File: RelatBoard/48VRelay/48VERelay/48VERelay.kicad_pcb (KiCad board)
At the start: 4 copper layers, 117 x 92 mm, 110 parts, among them J1 12, J10 Screw_Terminal_01x03, J11 Screw_Terminal_01x03, J12 Screw_Terminal_01x03, J13 Screw_Terminal_01x03, J14 Screw_Terminal_01x03, J2 RJ45_Hanrun_HR911105A_Horizon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, J3 B4B-PH-SM4-TB, J5 TC2030, K10 G2RL-1-E, K11 G2RL-1-E, K12 G2RL-1-E, K13 G2RL-1-E, K14 G2RL-1-E, U1 ESP32-WROOM-32UE, U10 TLV1117LV33DCYR, U2 ULN2803A, U3 W5500, U4 3A 32V, U5 TPS630701RNMR, U7 TVS1800DRVR, U9 TLV1117LV33DCYR, Y2 ABM3C-25.000MHZ-D4Y-T

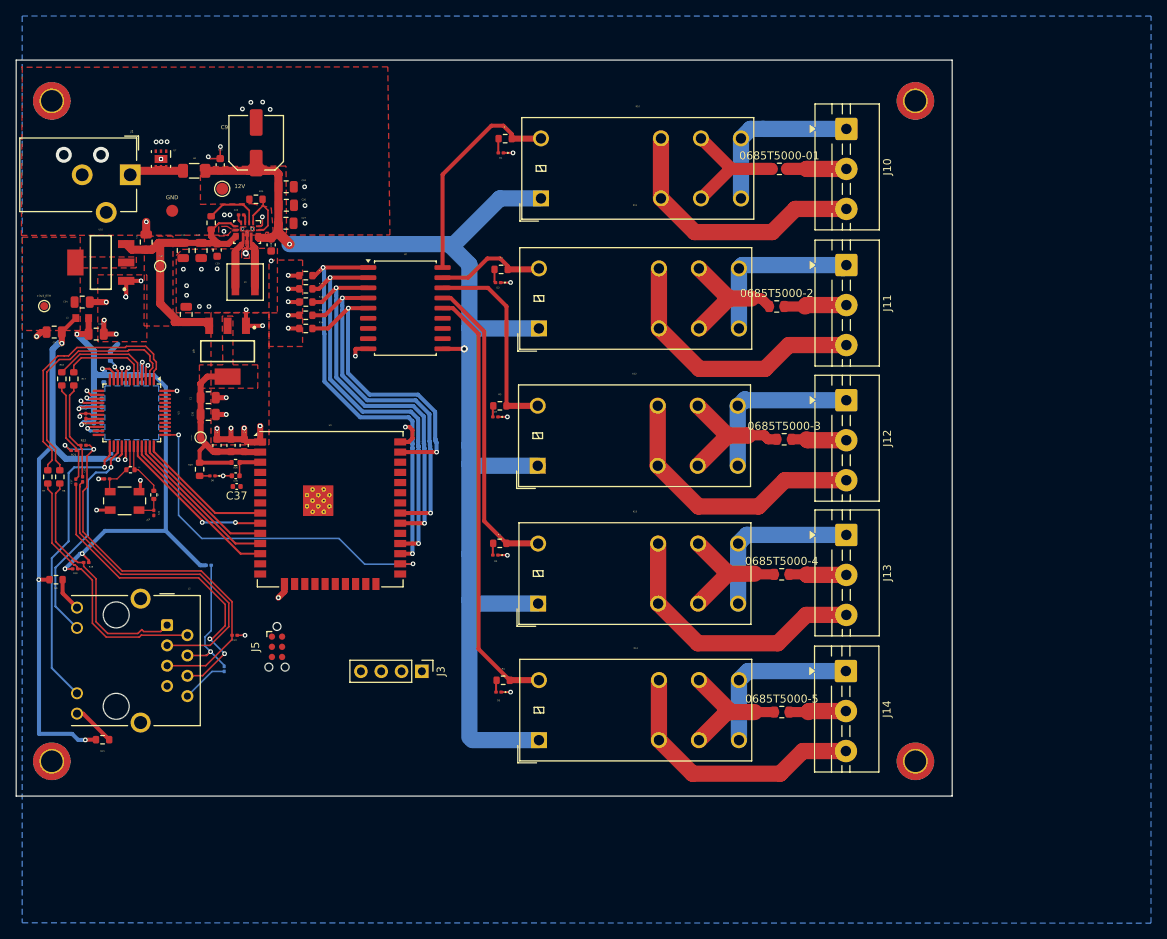
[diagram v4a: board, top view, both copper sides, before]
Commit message: wired uart and jtag
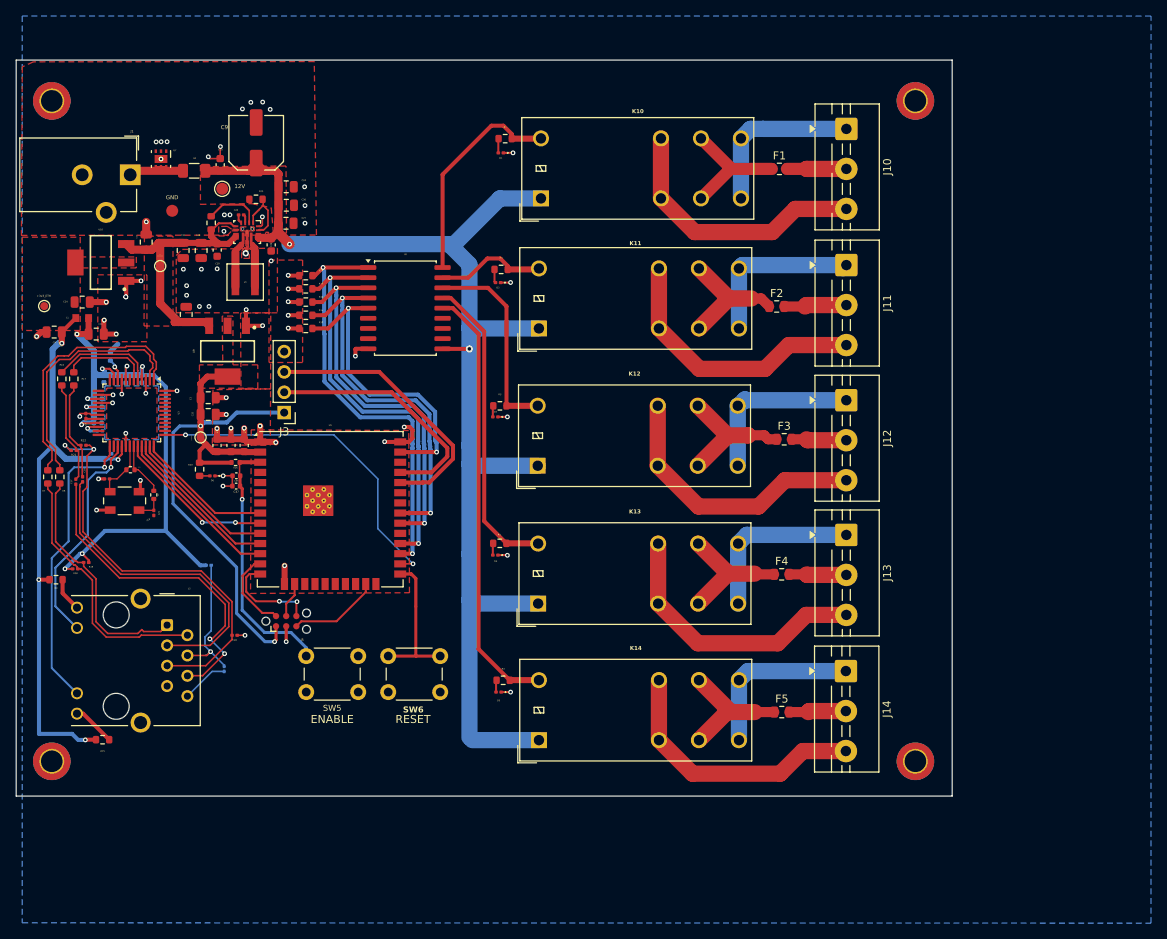
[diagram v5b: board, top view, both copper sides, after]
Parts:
- added SW5: ENABLE, Button_Switch_THT:SW_PUSH_6mm_H5mm, F.Cu at (82.8, 112.0)
- added SW6: RESET, Button_Switch_THT:SW_PUSH_6mm_H5mm, F.Cu at (86.5, 107.5)
- F1: renamed from 0685T5000-01; value Fuse_Small -> 0685T5000
- F2: renamed from 0685T5000-2; value Fuse_Small -> 0685T5000
- F3: renamed from 0685T5000-3; value Fuse_Small -> 0685T5000-01
- F4: renamed from 0685T5000-4; value Fuse_Small -> 0685T5000-01
- F5: renamed from 0685T5000-5; value Fuse_Small -> 0685T5000
- moved J3 36.6 mm to (73.5, 77.1), turned to 180 degrees
- moved J5 3.41 mm to (73.8, 103.1), turned to 0 degrees
- moved C36 0.08 mm to (67.5, 85.0)
- moved C37 0.08 mm to (67.5, 86.2)
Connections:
- C1 pad 1: JTAG_VREF -> 3V3 MCU
- C2 pad 1: JTAG_VREF -> 3V3 MCU
- C3 pad 1: JTAG_VREF -> 3V3 MCU
- C35 pad 1: JTAG_VREF -> 3V3 MCU
- C4 pad 1: JTAG_VREF -> 3V3 MCU
- J3 pad 1: +3V3 -> 3V3 MCU
- J5 pad 1: JTAG_VREF -> 3V3 MCU
- J5 pad 3: JTAG_GND -> GND
- R26 pad 1: JTAG_VREF -> 3V3 MCU
- R29 pad 1: JTAG_VREF -> 3V3 MCU
- U1 pad 2: JTAG_VREF -> 3V3 MCU
- U9 pad 2: JTAG_VREF -> 3V3 MCU
- U9 pad 4: JTAG_VREF -> 3V3 MCU
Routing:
- net 3V3 MCU: track 0.00 -> 76.2 mm, vias 0 -> 2
- net UART_RXD: track 0.00 -> 34.4 mm
- net UART_TXD: track 0.00 -> 31.1 mm
- net Net-(U1-EN): track 4.08 -> 32.2 mm, vias 0 -> 1
- net JTAG_VREF: track 27.2 -> 0.00 mm
- net Net-(U1-IO0): track 0.00 -> 18.4 mm
- net JTAG_TDI: track 0.00 -> 12.4 mm, vias 0 -> 2
- net JTAG_TDO: track 0.00 -> 11.5 mm
- net JTAG_TMS: track 0.00 -> 10.4 mm
- net GND: track 87.7 -> 96.1 mm, vias 71 -> 73
- net JTAG_TCK: track 0.00 -> 4.45 mm
- net +3V3A: track 88.4 -> 85.2 mm
- net /MCU/Ether_RESET: track 45.2 -> 42.9 mm
- net +12V: track 169.5 -> 170.1 mm
- added copper zone on F.Cu, net 3V3 MCU
- removed copper zone on F.Cu, net (none)

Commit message: update layout to include images
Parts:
- added G***: LOGO, LOGO, F.Cu at (69.5, 118.0)
- added G***: LOGO, LOGO, F.Cu at (85.0, 38.5)
- 3V3 MCU: renamed from +3V3 MCU
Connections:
- 3V3 MCU pad 1: (no net) -> 3V3 MCU
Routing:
- net Net-(U1-EN): track 32.2 -> 38.7 mm
- net GND: track 96.1 -> 97.0 mm, vias 73 -> 74
- net Net-(U5-EN): track 9.40 -> 8.85 mm

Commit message: Order1
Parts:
- added 3V3 Eth: TestPoint_Pad_D1.0mm, TestPoint:TestPoint_Pad_D1.0mm, B.Cu at (44.5, 78.2)
- added 3V3A: TestPoint_Pad_D1.0mm, TestPoint:TestPoint_Pad_D1.0mm, B.Cu at (49.8, 70.2)
- D1, D2, D3, D4, D5: footprint LED_SMD:LED_0201_0603Metric -> LED_SMD:LED_0805_2012Metric
- D6: footprint LED_SMD:LED_0201_0603Metric -> LED_SMD:LED_0603_1608Metric
- F1, F2, F3, F4, F5: footprint Fuse:Fuse_0805_2012Metric -> Fuse:Fuse_1206_3216Metric
- moved J14 10.1 mm to (143.7, 119.5), turned to 90 degrees
- moved J10 9.90 mm to (143.5, 51.5), turned to 90 degrees
- moved J11 9.88 mm to (143.8, 68.5), turned to 90 degrees
- moved J13 9.65 mm to (143.8, 102.0), turned to 90 degrees
- moved J12 9.48 mm to (143.8, 85.0), turned to 90 degrees
- moved R29 1.34 mm to (61.8, 83.5)
- moved D3 1.05 mm to (100.7, 78.2), turned to 0 degrees
- moved D5 0.87 mm to (100.8, 112.8), turned to 0 degrees
- moved D4 0.86 mm to (100.5, 95.5), turned to 0 degrees
- moved D2 0.86 mm to (100.8, 61.5), turned to 0 degrees
- moved C32 0.79 mm to (56.5, 55.0)
- moved G*** 0.71 mm to (70.0, 118.5)
- moved F2 0.69 mm to (135.8, 63.8)
- moved D1 0.45 mm to (101.0, 44.8), turned to 0 degrees
- moved F1 0.35 mm to (135.8, 46.6)
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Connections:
- D1 pad 1: GND -> Net-(D1-K)
- D1 pad 2: Net-(D1-A) -> +12V
- D2 pad 1: GND -> Net-(D2-K)
- D2 pad 2: Net-(D2-A) -> +12V
- D3 pad 1: GND -> Net-(D3-K)
- D3 pad 2: Net-(D3-A) -> +12V
- D4 pad 1: GND -> Net-(D4-K)
- D4 pad 2: Net-(D4-A) -> +12V
- D5 pad 1: GND -> Net-(D5-K)
- D5 pad 2: Net-(D5-A) -> +12V
- R1 pad 1: Net-(D1-A) -> Net-(D1-K)
- R2 pad 1: Net-(D2-A) -> Net-(D2-K)
- R3 pad 1: Net-(D3-A) -> Net-(D3-K)
- R4 pad 1: Net-(D5-A) -> Net-(D5-K)
- R5 pad 1: Net-(D4-A) -> Net-(D4-K)
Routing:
- net +12V: track 170.1 -> 202.3 mm, vias 2 -> 7
- net GND: track 97.0 -> 101.1 mm, vias 74 -> 71
- net Net-(D5-K): track 0.00 -> 2.42 mm
- net Net-(D2-K): track 0.00 -> 2.35 mm
- net Net-(D3-K): track 0.00 -> 2.17 mm
- net Net-(D1-K): track 0.00 -> 2.08 mm
- net 3V3 MCU: track 76.2 -> 78.1 mm
- net Net-(D1-A): track 1.80 -> 0.00 mm
- net Net-(D2-A): track 1.70 -> 0.00 mm
- net /Outputs/Relay_3: track 25.3 -> 23.8 mm
- net Net-(D5-A): track 1.50 -> 0.00 mm
- net Net-(D4-K): track 0.00 -> 1.49 mm
- net Net-(D4-A): track 1.49 -> 0.00 mm
- net Net-(D3-A): track 1.40 -> 0.00 mm
- net Net-(D6-A): track 1.31 -> 2.49 mm
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
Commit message: Fixed jtag, fixed diff pair routing, removed fuses
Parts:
- removed F1, F2, F5: 0685T5000, Fuse:Fuse_1206_3216Metric
- removed F3, F4: 0685T5000-01, Fuse:Fuse_1206_3216Metric
- removed the G*** at (85.0, 38.5)
- removed J5: TC2030, Connector:Tag-Connect_TC2030-IDC-NL_2x03_P1.27mm_Vertical
- added J4: TC2050, Connector:Tag-Connect_TC2050-IDC-NL_2x05_P1.27mm_Vertical, F.Cu at (79.2, 105.7)
- 3V3 Eth: moved to F.Cu
- 3V3A: moved to F.Cu
- moved R16 24.9 mm to (52.8, 96.8), turned to 0 degrees
- moved R6 24.5 mm to (51.7, 94.5), turned to 180 degrees
- moved R17 23.1 mm to (52.8, 95.2), turned to 0 degrees
- moved C12 20.5 mm to (48.5, 92.0), turned to 90 degrees
- moved R20 20.3 mm to (46.2, 106.0), turned to -90 degrees
- moved C6 19.8 mm to (46.2, 107.9)
- moved C13 19.4 mm to (53.2, 92.0), turned to 90 degrees
- moved C15 19.4 mm to (50.5, 92.0), turned to 90 degrees
- moved C21 17.6 mm to (47.0, 75.2), turned to 90 degrees
- moved R21 17.2 mm to (55.0, 97.2), turned to -90 degrees
- moved R22 15.3 mm to (55.0, 95.0), turned to 90 degrees
- moved C16 14.6 mm to (54.0, 89.5), turned to 180 degrees
- moved R23 14.2 mm to (47.0, 77.5), turned to 90 degrees
- moved C17 14.1 mm to (56.2, 96.8), turned to 0 degrees
- moved C14 12.7 mm to (54.0, 88.5), turned to 180 degrees
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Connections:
- K10 pad 11: Net-(F1-Pad1) -> /Outputs/COM_1
- K11 pad 11: Net-(F2-Pad1) -> /Outputs/COM_2
- K12 pad 11: Net-(F3-Pad1) -> /Outputs/COM_3
- K13 pad 11: Net-(F4-Pad1) -> /Outputs/COM_4
- K14 pad 11: Net-(F5-Pad1) -> /Outputs/COM_5
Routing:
- net /MCU/Ether_RESET: track 42.9 -> 82.8 mm
- net /MCU/Ether_INT: track 17.2 -> 53.5 mm, vias 0 -> 2
- net /MCU/Ether_MOSI: track 18.8 -> 53.4 mm, vias 0 -> 2
- net /MCU/Ether_MISO: track 19.9 -> 52.7 mm, vias 0 -> 2
- net /MCU/Ether_SCLK: track 21.0 -> 52.5 mm, vias 0 -> 2
- net RX_CT: track 53.4 -> 21.9 mm
- net GND: track 101.1 -> 131.9 mm, vias 71 -> 157
- net /MCU/Ether_CS: track 20.2 -> 49.6 mm
- net /MCU/PHY_R_TXN: track 32.1 -> 3.26 mm
- net /MCU/PHY_R_TXP: track 30.6 -> 2.87 mm
- net RX_N: track 42.2 -> 19.2 mm, vias 2 -> 0
- net RX_P: track 40.5 -> 19.1 mm
- net /Outputs/COM_2: track 6.69 -> 25.8 mm
- net /Outputs/COM_3: track 6.37 -> 25.5 mm
- net /Outputs/COM_5: track 6.67 -> 25.5 mm
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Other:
- board text added: "220V AC 16A MAX"
- board text added: "5 Channel Relay"
- board text added: "52V DC 2.5A MAX"
- board text added: "Qilon"
